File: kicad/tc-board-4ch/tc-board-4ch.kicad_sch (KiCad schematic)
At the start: 6 parts, among them J1 HOST, J2 BUTTON, U1 SN74AHC125DR

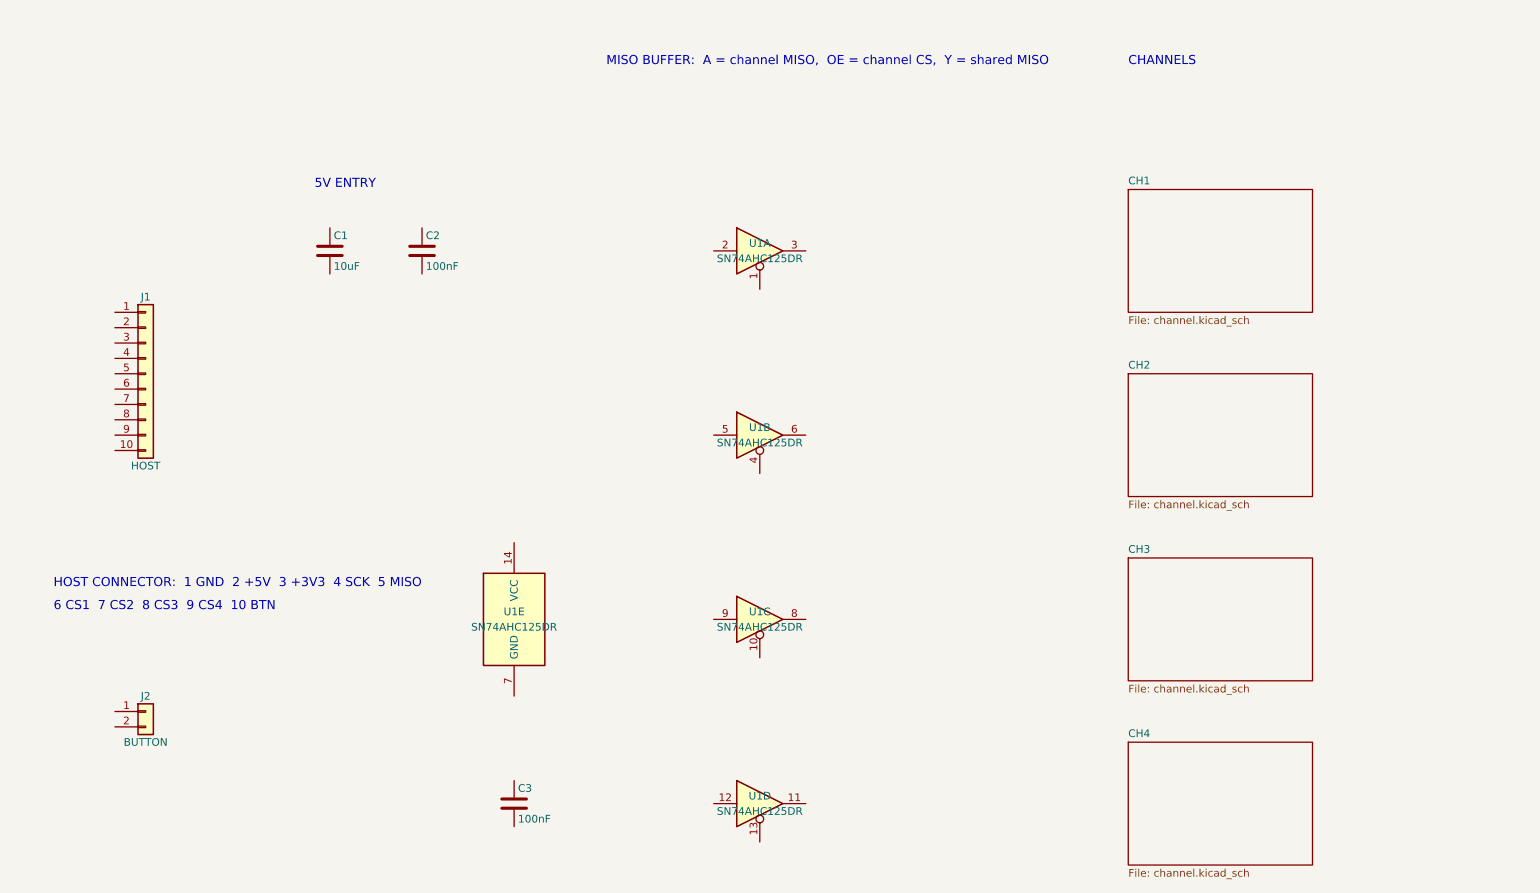
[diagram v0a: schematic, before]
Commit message: Schematic session 2: 4-channel isolated board ERC-clean
- Channel sheet: probe input chain (TVS, ferrite, 1 nF, 10 nF differential)
- Root sheet: sheet pins, host connector, 5V entry, SN74AHC125 MISO buffer,
  button connector, PWR_FLAGs
- ERC reports zero violations on all five sheets
- Roll the 2 Oct session into the archive; next step is the footprint check
  and PCB layout

Co-Authored-By: Claude Fable 5.1 <noreply@anthropic.com>
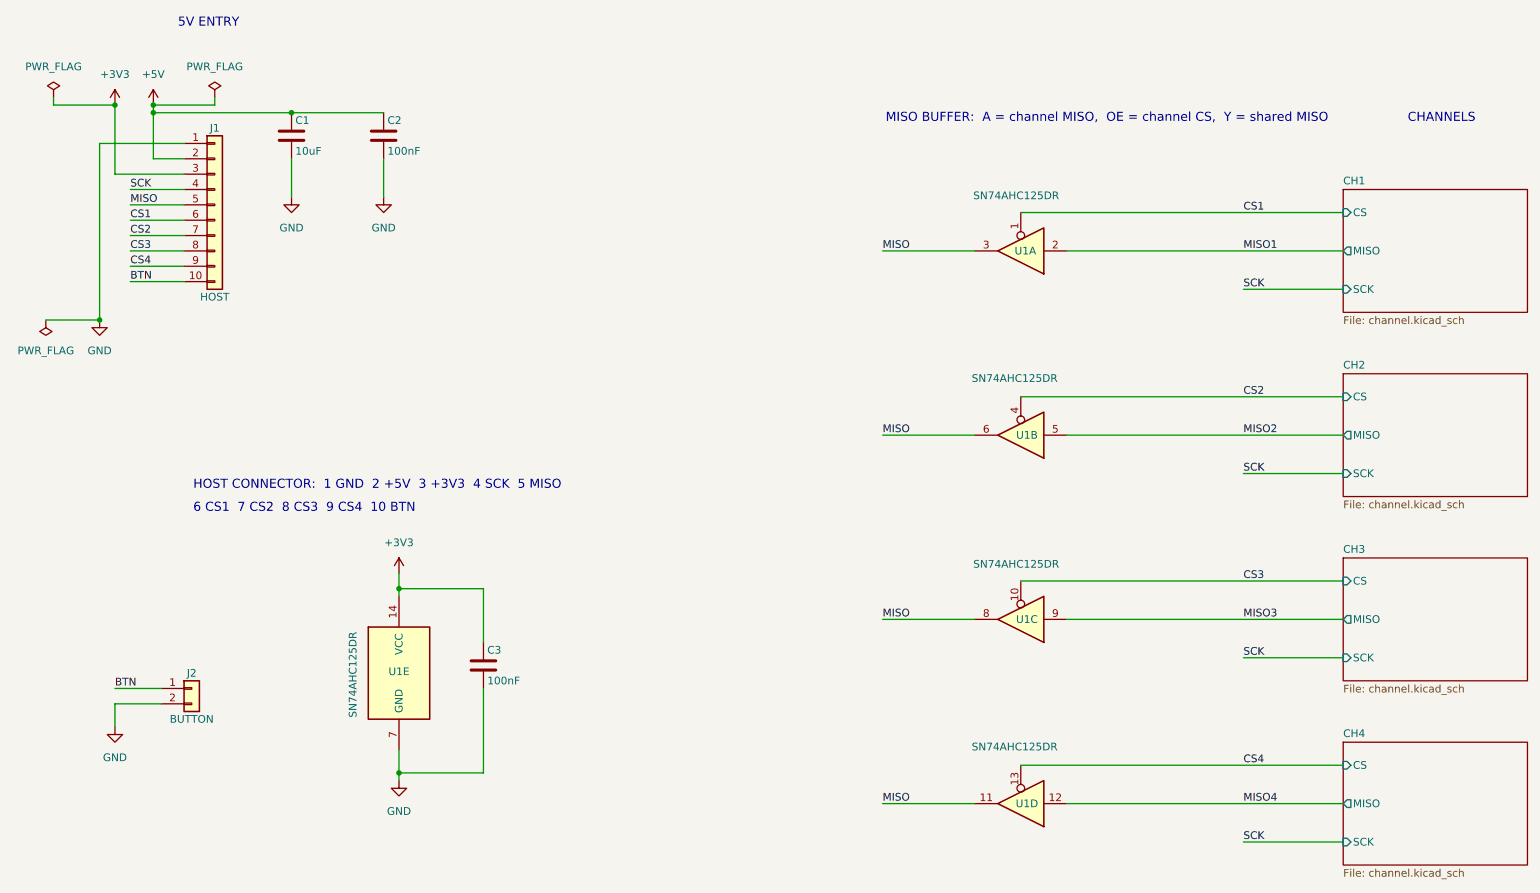
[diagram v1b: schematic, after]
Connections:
- net BTN: now reaches J2.1 (Pin_1)
- net BTN: now also J1.10 (Pin_10)
- net GND: now reaches J2.2 (Pin_2)
- net GND: now also C1.2, C2.2, C3.2, J1.1 (Pin_1), U1.7 (GND)
- net +5V: now reaches J1.2 (Pin_2)
- net +5V: now also C1.1, C2.1
- net +3V3: now reaches J1.3 (Pin_3)
- net +3V3: now also C3.1, U1.14 (VCC)
- net SCK: now reaches J1.4 (Pin_4)
- net MISO: now reaches J1.5 (Pin_5)
- net MISO: now also U1.11, U1.3, U1.6, U1.8
- net CS1: now reaches J1.6 (Pin_6)
- net CS1: now also U1.1
- net CS2: now reaches J1.7 (Pin_7)
- net CS2: now also U1.4
- net CS3: now reaches J1.8 (Pin_8)
- net CS3: now also U1.10
- net CS4: now reaches J1.9 (Pin_9)
- net CS4: now also U1.13
- net MISO2: now reaches U1.5
- net MISO4: now reaches U1.12
- net MISO3: now reaches U1.9
- net MISO1: now reaches U1.2
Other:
- sheet CH1 ports: added CS, MISO, SCK; removed none
- sheet CH2 ports: added CS, MISO, SCK; removed none
- sheet CH3 ports: added CS, MISO, SCK; removed none
- sheet CH4 ports: added CS, MISO, SCK; removed none
- moved on the sheet: C1, C2, C3, J1, J2, U1A, U1B, U1C, U1D, U1E
